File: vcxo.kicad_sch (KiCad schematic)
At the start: 27 parts, among them U901 DAC8551, U902 MCP1501-33xSN, U903 NCS325, U904 74LVC2GU04, U905 74LVC2G04, X901 TXEAADSANF-20.0, X902 DOT050V-020.0M

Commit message: Assign WP130WCP and DTO050 footprints in schematic
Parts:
- X902: footprint (none) -> custom-footprints:ConnorWinfield_DOT050
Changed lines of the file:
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@@
       (effects (font (size 1.27 1.27)) (justify left))
     )
-    (property "Footprint" "" (id 2) (at 170.18 133.35 0)
+    (property "Footprint" "custom-footprints:ConnorWinfield_DOT050" (id 2) (at 170.18 133.35 0)
       (effects (font (size 1.27 1.27)) hide)
     )

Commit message: Update footprints: - SOD323F, SOD323, SOD123W... intead of generic handsolder version - 3225 xtal - use handsolder footprint - do not use handsolder version for ferrite beads - use SOT-23-6 instead of TSOP-6
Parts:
- FB901: footprint Inductor_SMD:L_0805_2012Metric_Pad1.05x1.20mm_HandSolder -> Inductor_SMD:L_0805_2012Metric
- X901: footprint Crystal:Crystal_SMD_3225-4Pin_3.2x2.5mm -> Crystal:Crystal_SMD_3225-4Pin_3.2x2.5mm_HandSoldering
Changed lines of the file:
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@@
     (property "Reference" "FB901" (id 0) (at 95.1992 20.3286 90))
     (property "Value" "782853701" (id 1) (at 95.1992 22.8655 90))
-    (property "Footprint" "Inductor_SMD:L_0805_2012Metric_Pad1.05x1.20mm_HandSolder" (id 2) (at 95.25 28.448 90)
+    (property "Footprint" "Inductor_SMD:L_0805_2012Metric" (id 2) (at 95.25 28.448 90)
       (effects (font (size 1.27 1.27)) hide)
     )
@@
     (property "Reference" "X901" (id 0) (at 176.53 88.9 0))
     (property "Value" "TXEAADSANF-20.0" (id 1) (at 182.88 91.44 0))
-    (property "Footprint" "Crystal:Crystal_SMD_3225-4Pin_3.2x2.5mm" (id 2) (at 170.18 99.06 0)
-      (effects (font (size 1.27 1.27)) hide)
-    )
+    (property "Footprint" "Crystal:Crystal_SMD_3225-4Pin_3.2x2.5mm_HandSoldering" (id 2) (at 170.18 99.06 0)
+      (effects (font (size 1.27 1.27)) hide)
+    )

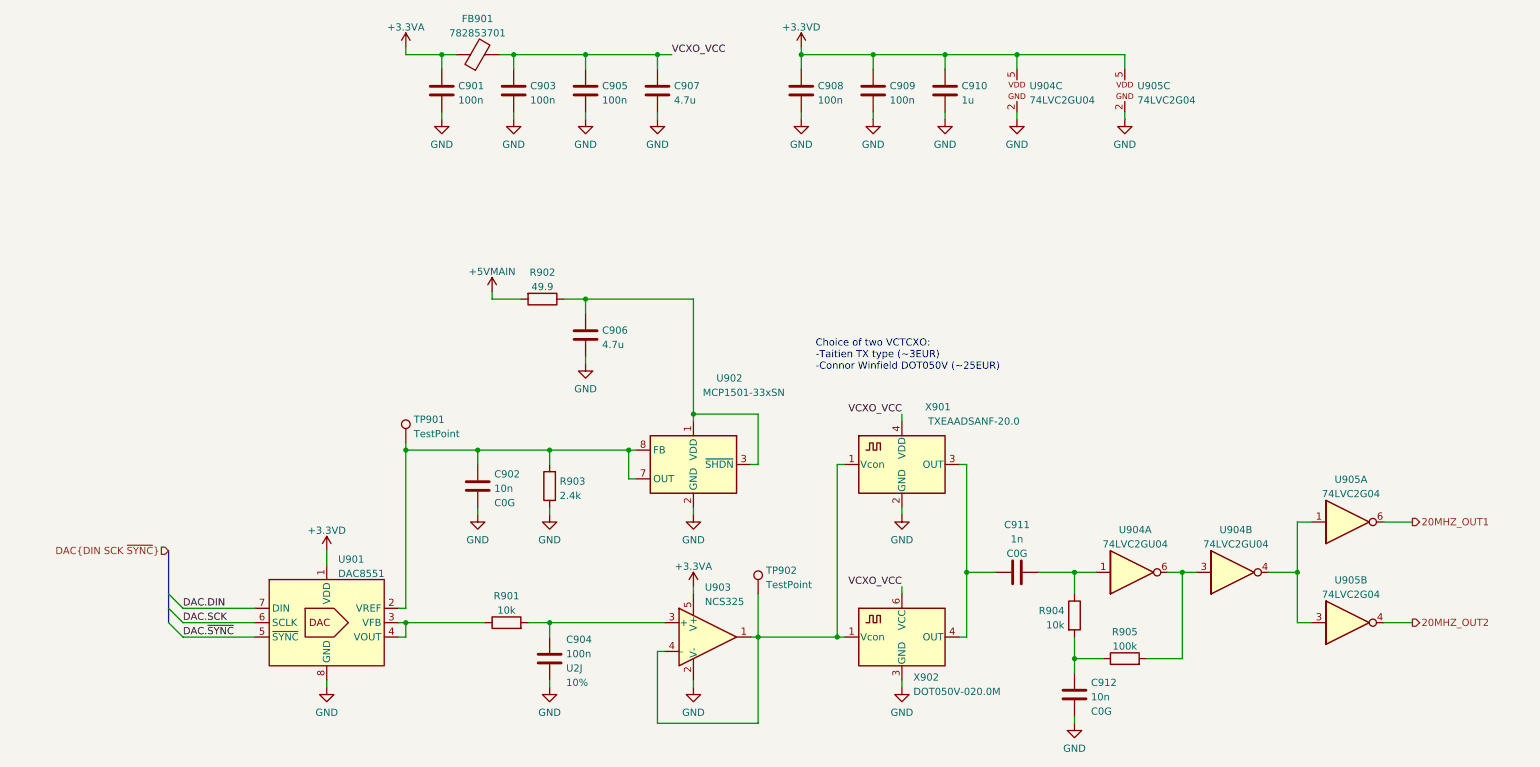
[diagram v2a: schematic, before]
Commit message: Reconnect some things to simplify PCB routing
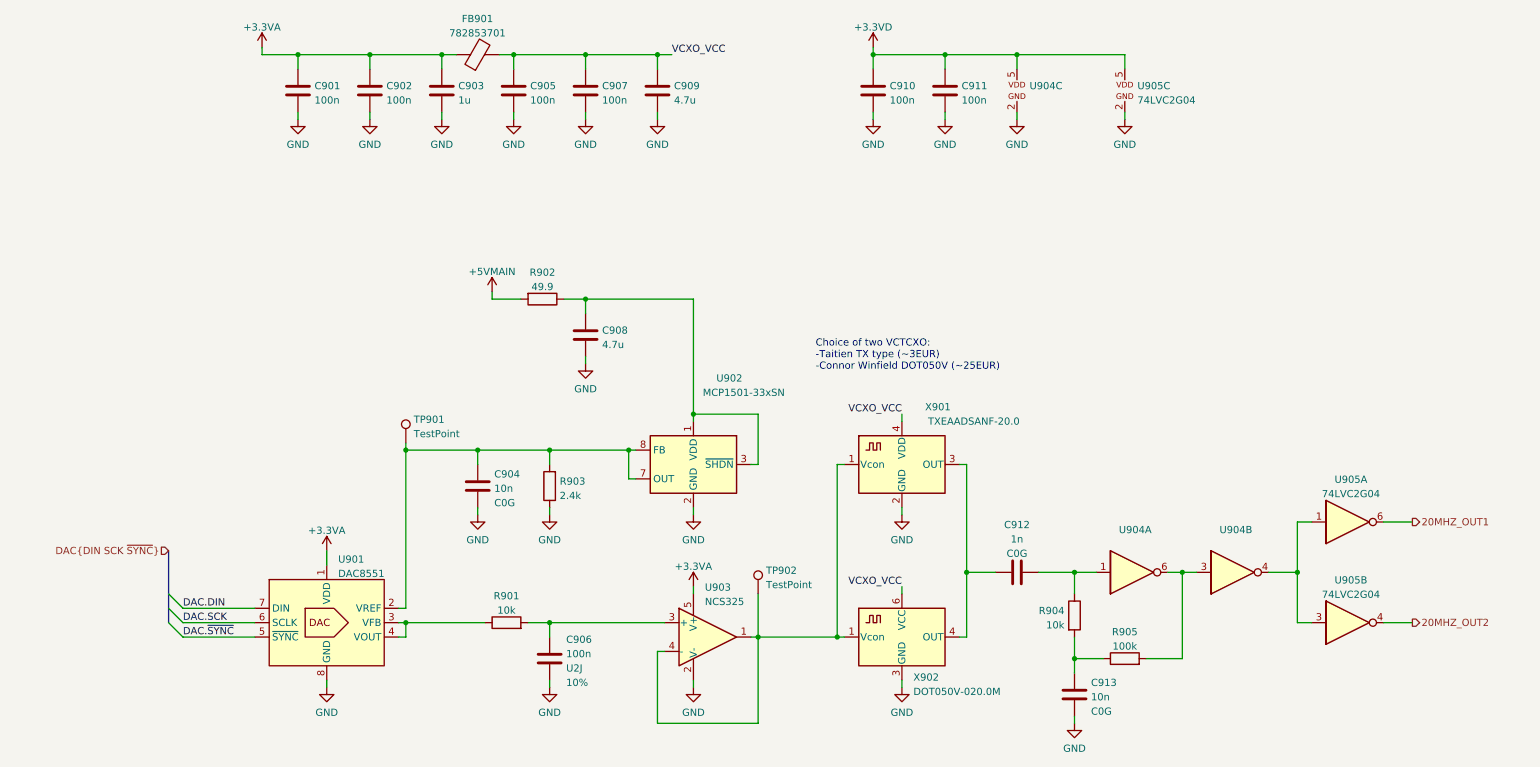
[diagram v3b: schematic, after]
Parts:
- added C901: 100n, Capacitor_SMD:C_0805_2012Metric, symbol Device:C
- U904: value 74LVC2GU04 -> (none); footprint Package_TO_SOT_SMD:SOT-23-6 -> (none)
- renumbered C901 to C902, C910 to C903, C902 to C904, C903 to C905, C904 to C906, C905 to C907, C906 to C908, C907 to C909, C908 to C910, C909 to C911, C911 to C912, C912 to C913
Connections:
- net +3.3VA: now also C903.2, U901.1 (VDD), C901.2
- net +3.3VD: no longer C903.2, U901.1 (VDD)
- net GND: now also C901.1
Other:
- moved on the sheet: C902, C903, C910, C911

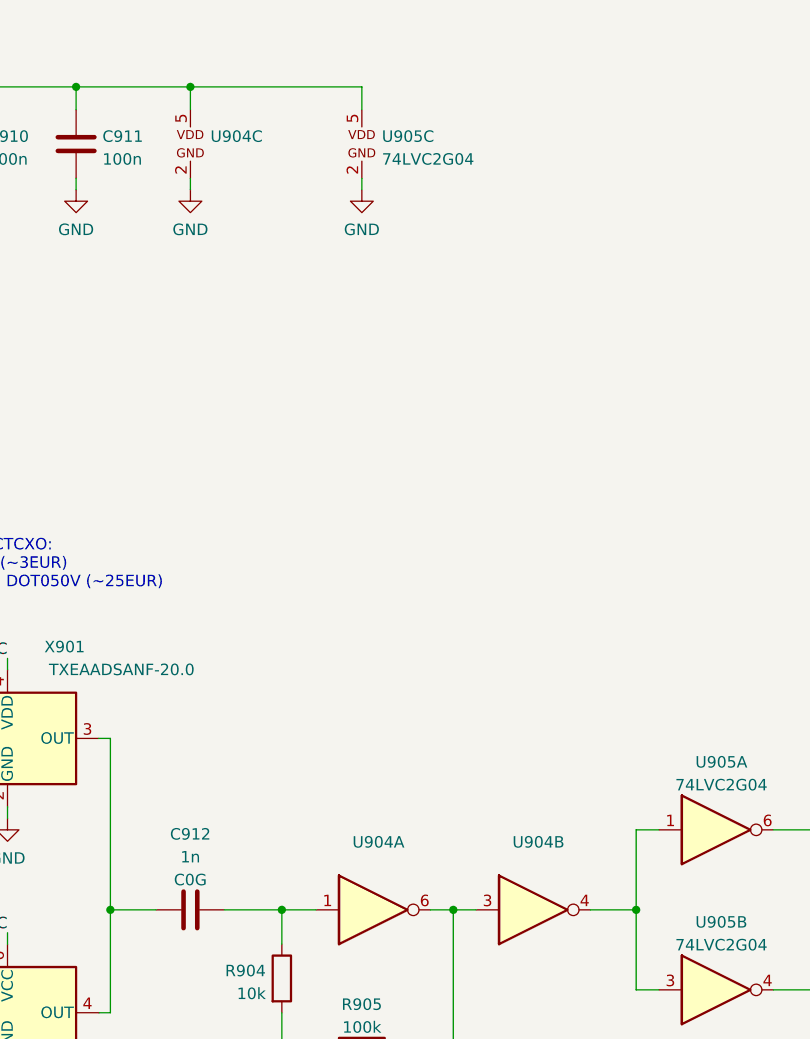
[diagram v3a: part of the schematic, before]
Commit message: Fix footprints, values and PNs
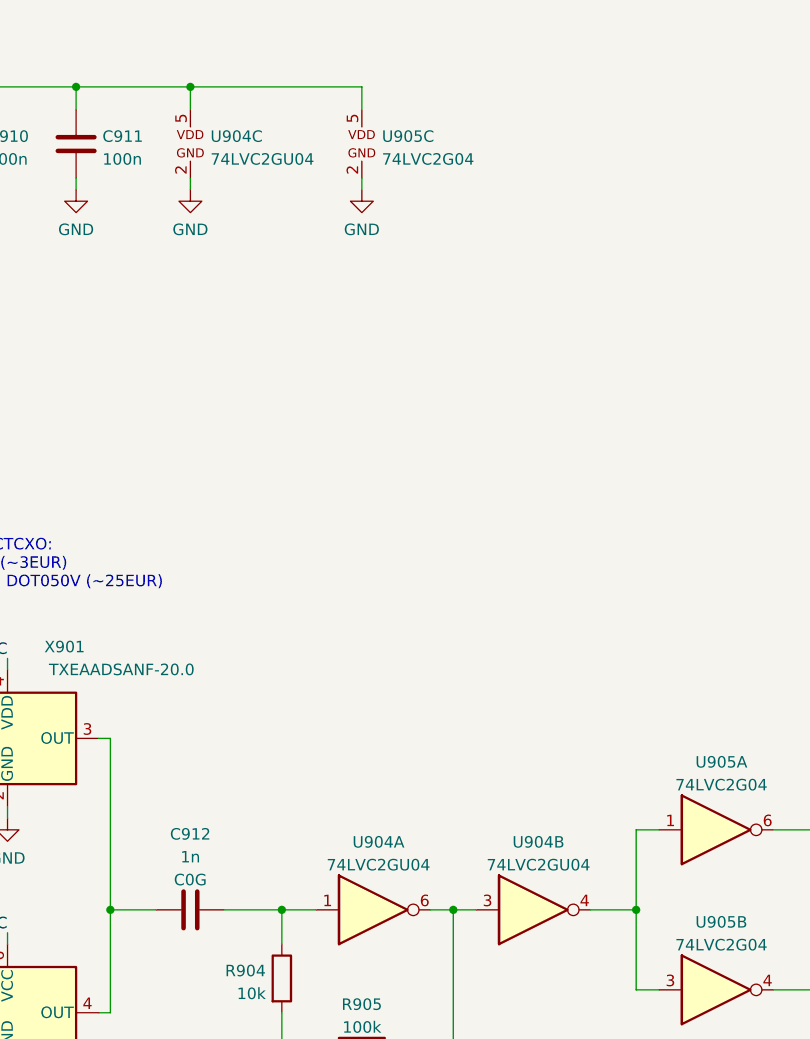
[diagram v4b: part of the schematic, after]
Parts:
- U904: value (none) -> 74LVC2GU04; footprint (none) -> Package_TO_SOT_SMD:SOT-23-6
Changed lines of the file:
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@@
     (in_bom yes) (on_board yes) (fields_autoplaced)
     (property "Reference" "U904" (id 0) (at 229.1715 110.6002 0))
-    (property "Value" "" (id 1) (at 229.1715 113.1371 0))
-    (property "Footprint" "" (id 2) (at 227.33 100.33 0)
+    (property "Value" "74LVC2GU04" (id 1) (at 229.1715 113.1371 0))
+    (property "Footprint" "Package_TO_SOT_SMD:SOT-23-6" (id 2) (at 227.33 100.33 0)
       (effects (font (size 1.27 1.27)) hide)
     )
@@
       (effects (font (size 1.27 1.27)) (justify left))
     )
-    (property "Value" "" (id 1) (at 192.7213 34.7222 0)
-      (effects (font (size 1.27 1.27)) (justify left))
-    )
-    (property "Footprint" "" (id 2) (at 190.5 15.24 0)
+    (property "Value" "74LVC2GU04" (id 1) (at 192.7213 34.7222 0)
+      (effects (font (size 1.27 1.27)) (justify left))
+    )
+    (property "Footprint" "Package_TO_SOT_SMD:SOT-23-6" (id 2) (at 190.5 15.24 0)
       (effects (font (size 1.27 1.27)) hide)
     )
@@
     (in_bom yes) (on_board yes) (fields_autoplaced)
     (property "Reference" "U904" (id 0) (at 211.3915 110.6002 0))
-    (property "Value" "" (id 1) (at 211.3915 113.1371 0))
-    (property "Footprint" "" (id 2) (at 209.55 100.33 0)
-      (effects (font (size 1.27 1.27)) hide)
-    )
+    (property "Value" "74LVC2GU04" (id 1) (at 211.3915 113.1371 0))
+    (property "Footprint" "Package_TO_SOT_SMD:SOT-23-6" (id 2) (at 209.55 100.33 0)
+      (effects (font (size 1.27 1.27)) hide)
+    )

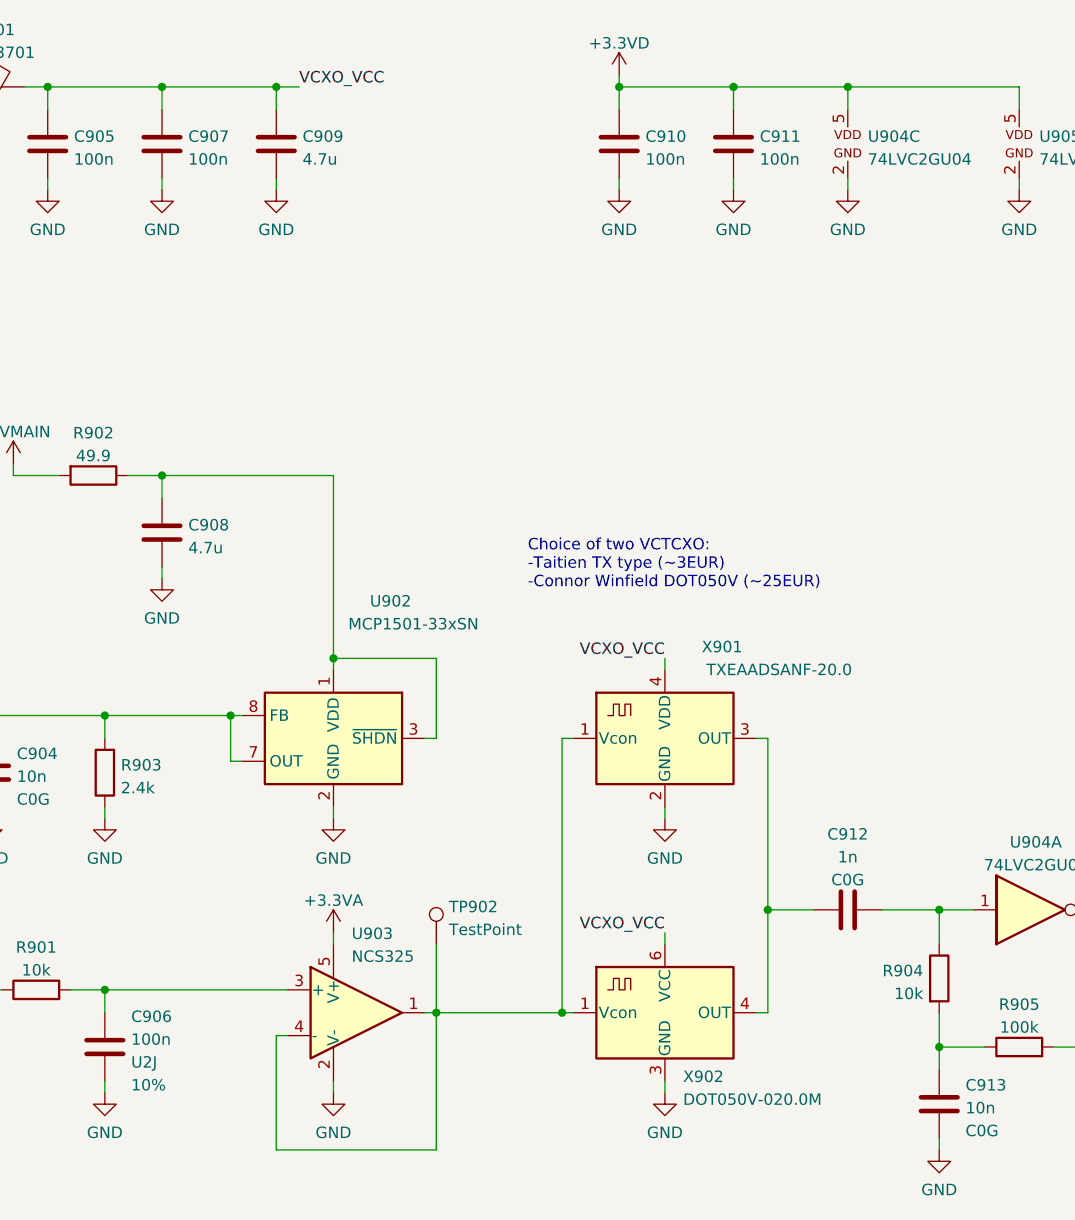
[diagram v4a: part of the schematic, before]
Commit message: VCXO: remove Taitien vctcxo, add extra decoupling
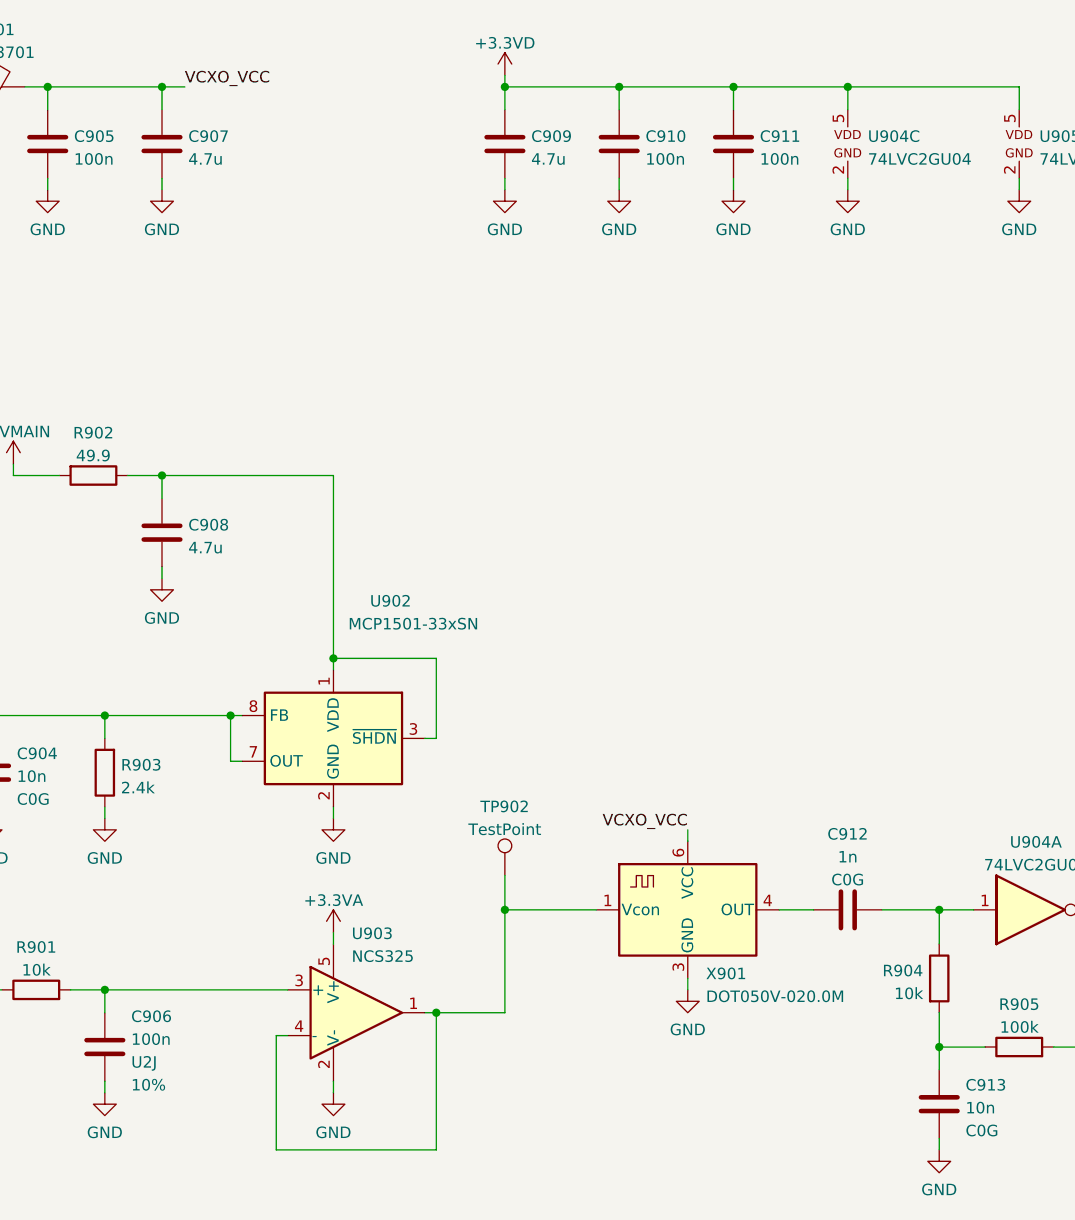
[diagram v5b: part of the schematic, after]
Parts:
- removed C907: 100n, Capacitor_SMD:C_0805_2012Metric, symbol Device:C
- removed X901: TXEAADSANF-20.0, Crystal:Crystal_SMD_3225-4Pin_3.2x2.5mm_HandSoldering, symbol symbols:TAITIEN-TX
- added C909: 4.7u, Capacitor_SMD:C_0805_2012Metric, symbol Device:C
- renumbered C909 to C907, X902 to X901
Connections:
- net +3.3VD: now also C909.2
- net GND: now also C909.1
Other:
- note removed: "Choice of two VCTCXO: -Taitien TX type (~3EUR) -Connor Winfield DOT050V (~25EUR)"
- moved on the sheet: C907, TP902, X901
